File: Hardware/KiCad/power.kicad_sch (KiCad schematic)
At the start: 54 parts, among them U6 TP6841S6, U7 TPS73233

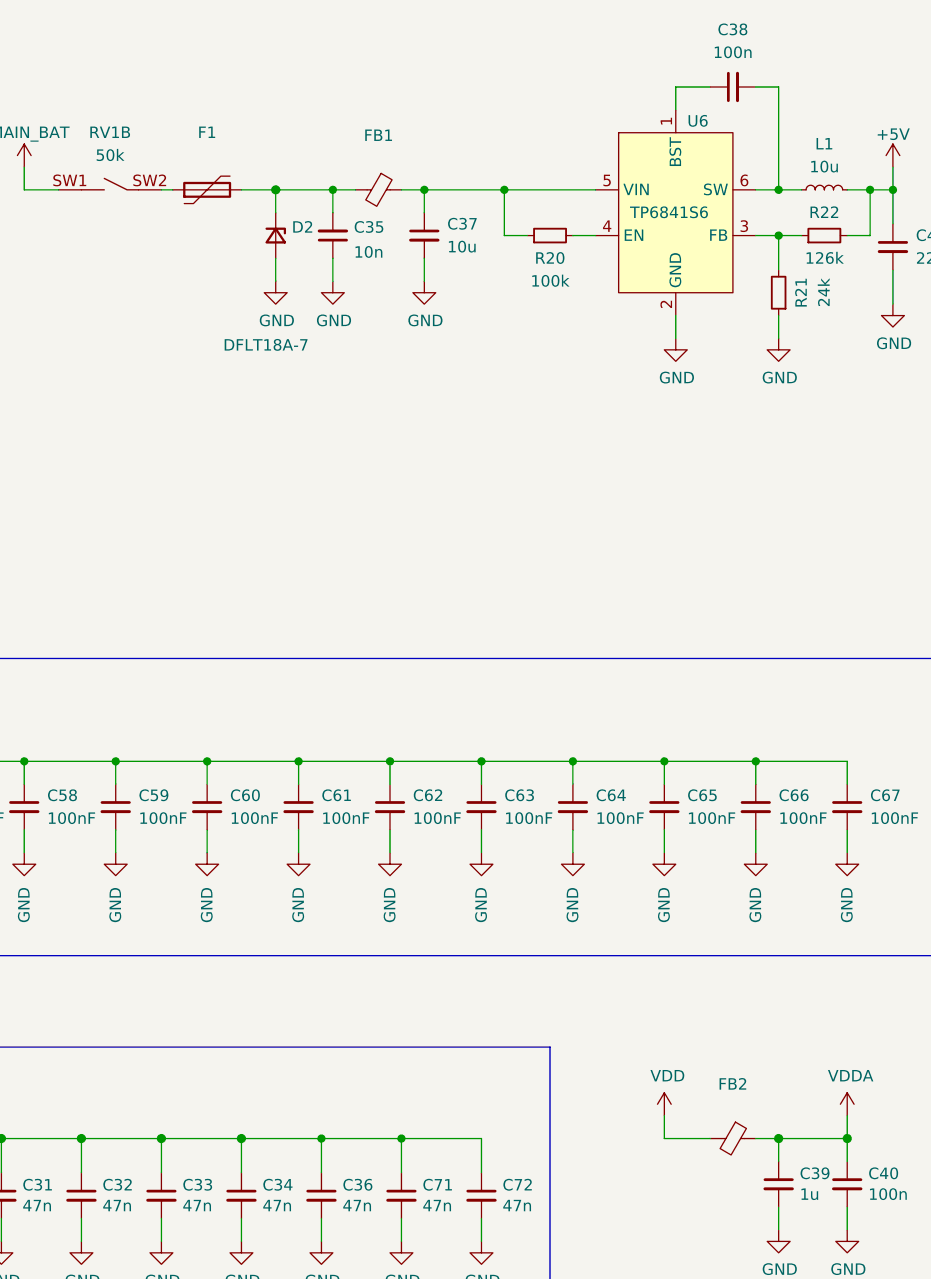
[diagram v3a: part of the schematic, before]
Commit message: move cc1200 spi to spi-5 & update other labels throughout
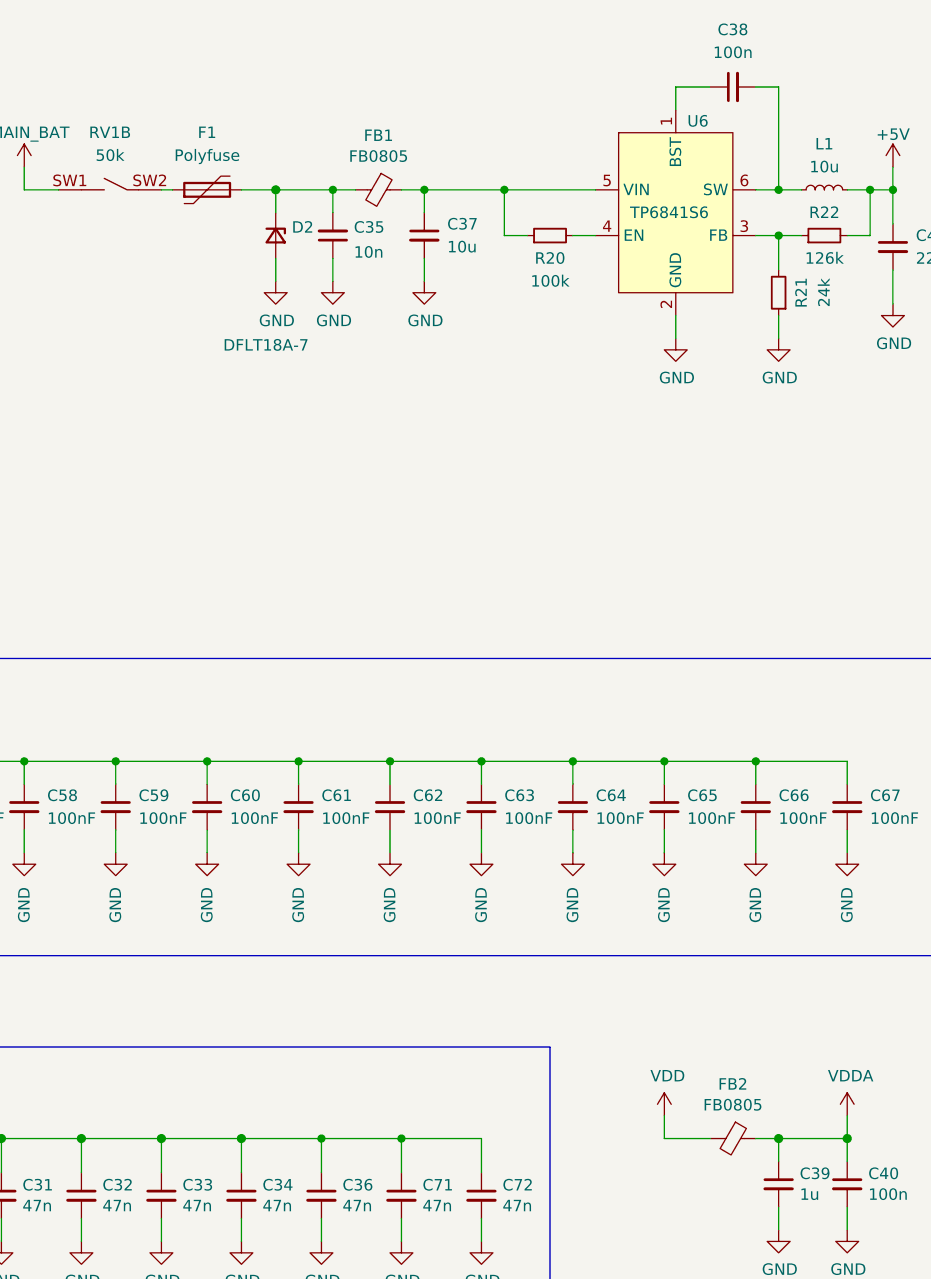
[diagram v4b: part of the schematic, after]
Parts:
- F1: value (none) -> Polyfuse; footprint (none) -> Fuse:Fuse_0805_2012Metric
- FB1, FB2: value (none) -> FB0805; footprint (none) -> Fuse:Fuse_0805_2012Metric
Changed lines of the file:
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@@
     (in_bom yes) (on_board yes)
     (property "Reference" "FB1" (id 0) (at 92.71 29.5402 90))
-    (property "Value" "" (id 1) (at 92.71 31.8516 90))
-    (property "Footprint" "" (id 2) (at 92.71 33.782 90)
+    (property "Value" "FB0805" (id 1) (at 92.71 31.8516 90))
+    (property "Footprint" "Fuse:Fuse_0805_2012Metric" (id 2) (at 92.71 33.782 90)
       (effects (font (size 1.27 1.27)) hide)
     )
@@
     (in_bom yes) (on_board yes) (fields_autoplaced)
     (property "Reference" "F1" (id 0) (at 73.66 29.21 90))
-    (property "Value" "" (id 1) (at 73.66 31.75 90))
-    (property "Footprint" "" (id 2) (at 78.74 34.29 0)
+    (property "Value" "Polyfuse" (id 1) (at 73.66 31.75 90))
+    (property "Footprint" "Fuse:Fuse_0805_2012Metric" (id 2) (at 78.74 34.29 0)
       (effects (font (size 1.27 1.27)) (justify left) hide)
     )
@@
     (in_bom yes) (on_board yes)
     (property "Reference" "FB2" (id 0) (at 132.08 134.9502 90))
-    (property "Value" "" (id 1) (at 132.08 137.2616 90))
-    (property "Footprint" "" (id 2) (at 132.08 139.192 90)
-      (effects (font (size 1.27 1.27)) hide)
-    )
+    (property "Value" "FB0805" (id 1) (at 132.08 137.2616 90))
+    (property "Footprint" "Fuse:Fuse_0805_2012Metric" (id 2) (at 132.08 139.192 90)
+      (effects (font (size 1.27 1.27)) hide)
+    )

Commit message: rough layout of cc1200
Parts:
- removed C29, C30, C31, C32, C33, C34, C36, C71, C72: 47n, Capacitor_SMD:C_0402_1005Metric, symbol pkl_device:pkl_C_Small
- C9: renamed from C61; value 100nF -> (none); footprint Capacitor_SMD:C_0402_1005Metric -> (none)
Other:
- note removed: "CC1200 decoupling"

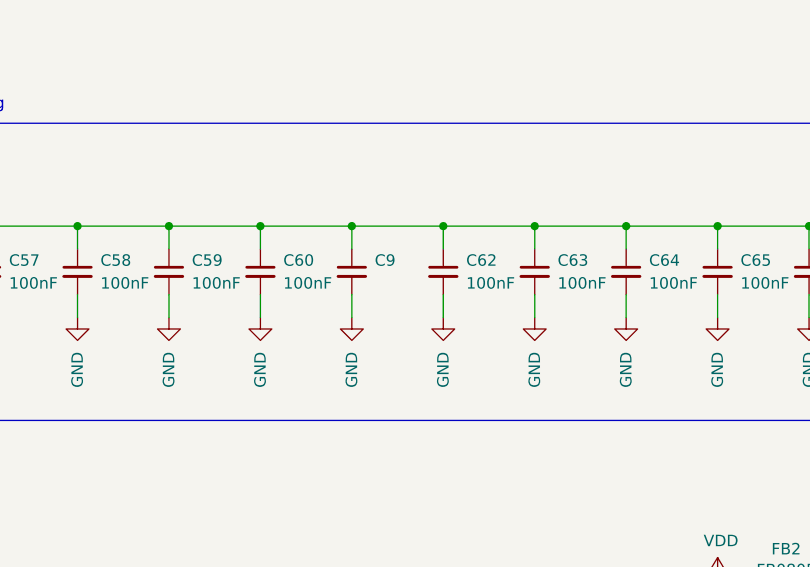
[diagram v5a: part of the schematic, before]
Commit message: fix issue 21 & 20 & move MCU to align w/ grid
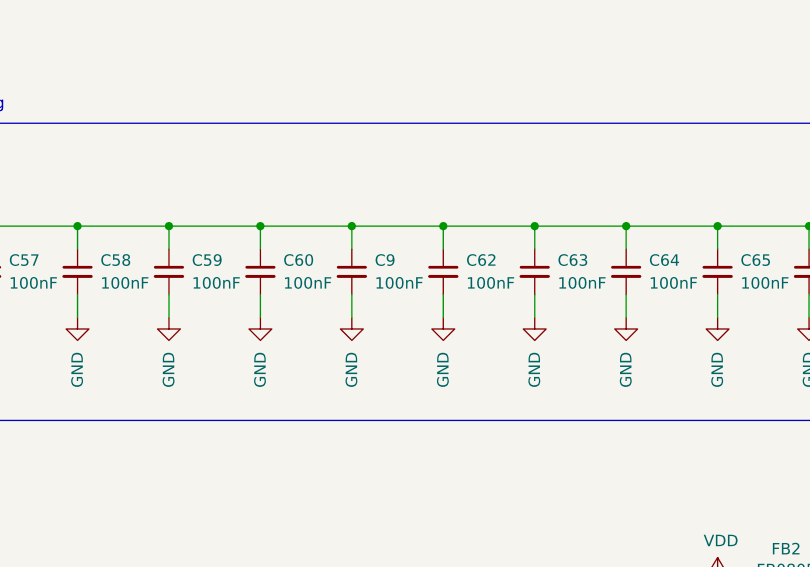
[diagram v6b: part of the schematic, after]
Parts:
- C9: value (none) -> 100nF; footprint (none) -> Capacitor_SMD:C_0402_1005Metric
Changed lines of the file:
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@@
       (effects (font (size 1.27 1.27)) (justify left))
     )
-    (property "Value" "" (id 1) (at 86.36 105.4162 0)
+    (property "Value" "100nF" (id 1) (at 86.36 105.4162 0)
       (effects (font (size 1.27 1.27)) (justify left))
     )
-    (property "Footprint" "" (id 2) (at 83.82 104.14 0)
+    (property "Footprint" "Capacitor_SMD:C_0402_1005Metric" (id 2) (at 83.82 104.14 0)
       (effects (font (size 1.27 1.27)) hide)
     )

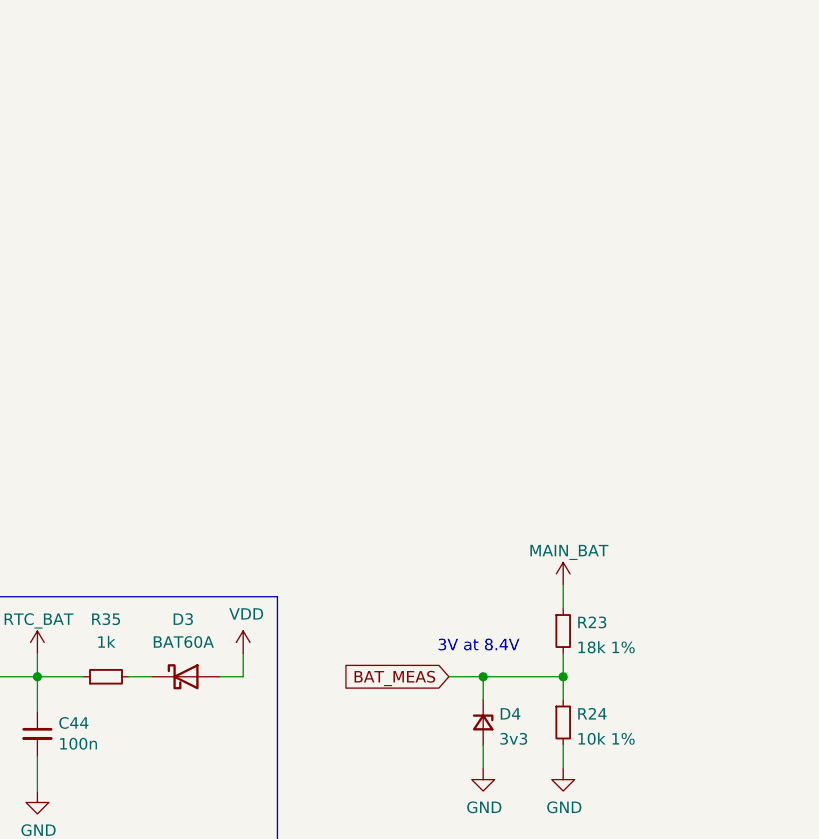
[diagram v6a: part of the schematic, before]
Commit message: Minor corrections
- fixed microphone connection and part values
- added a few TPs
- changed C27 footprint
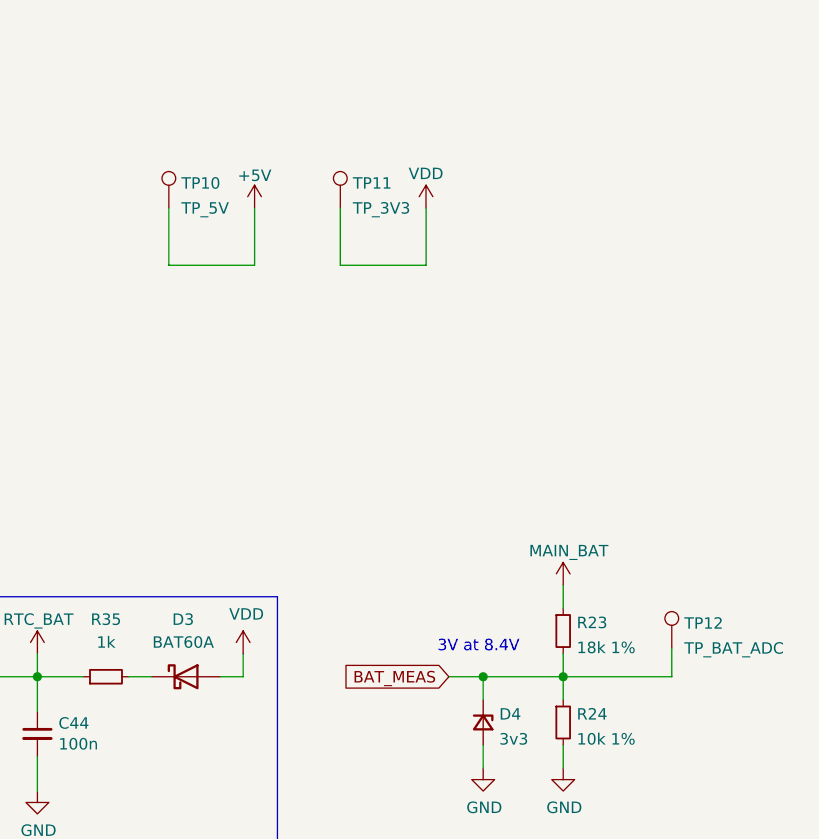
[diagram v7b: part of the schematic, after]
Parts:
- added TP10: TP_5V, TestPoint:TestPoint_Pad_D1.0mm, symbol Connector:TestPoint
- added TP11: TP_3V3, TestPoint:TestPoint_Pad_D1.0mm, symbol Connector:TestPoint
- added TP12: TP_BAT_ADC, TestPoint:TestPoint_Pad_D1.0mm, symbol Connector:TestPoint
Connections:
- net +5V: now also TP10.1
- net BAT_MEAS: now also TP12.1
- net VDD: now also TP11.1
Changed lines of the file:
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@@
     (stroke (width 0) (type solid) (color 0 0 0 0))
+  )
+  (wire (pts (xy 200.025 95.25) (xy 209.55 95.25))
+    (stroke (width 0) (type default) (color 0 0 0 0))
   )
   (wire (pts (xy 114.3 101.6) (xy 114.3 99.06))
@@
     (stroke (width 0) (type default) (color 0 0 0 0))
   )
+  (wire (pts (xy 200.025 88.9) (xy 200.025 95.25))
+    (stroke (width 0) (type default) (color 0 0 0 0))
+  )
+  (wire (pts (xy 255.905 137.795) (xy 255.905 140.97))
+    (stroke (width 0) (type default) (color 0 0 0 0))
+  )
   (wire (pts (xy 114.3 106.68) (xy 114.3 109.22))
     (stroke (width 0) (type default) (color 0 0 0 0))
@@
     (stroke (width 0) (type default) (color 0 0 0 0))
   )
+  (wire (pts (xy 228.6 95.25) (xy 228.6 88.9))
+    (stroke (width 0) (type default) (color 0 0 0 0))
+  )
   (wire (pts (xy 144.78 140.97) (xy 144.78 138.43))
     (stroke (width 0) (type solid) (color 0 0 0 0))
@@
     (stroke (width 0) (type default) (color 0 0 0 0))
   )
+  (wire (pts (xy 209.55 95.25) (xy 209.55 88.9))
+    (stroke (width 0) (type default) (color 0 0 0 0))
+  )
   (wire (pts (xy 104.14 99.06) (xy 114.3 99.06))
     (stroke (width 0) (type default) (color 0 0 0 0))
@@
     (stroke (width 0) (type solid) (color 0 0 0 0))
   )
+  (wire (pts (xy 219.075 88.9) (xy 219.075 95.25))
+    (stroke (width 0) (type default) (color 0 0 0 0))
+  )
   (wire (pts (xy 125.73 24.13) (xy 125.73 26.67))
     (stroke (width 0) (type default) (color 0 0 0 0))
   )
+  (wire (pts (xy 219.075 95.25) (xy 228.6 95.25))
+    (stroke (width 0) (type default) (color 0 0 0 0))
+  )
   (polyline (pts (xy 170.18 132.08) (xy 212.09 132.08))
     (stroke (width 0) (type default) (color 0 0 0 0))
@@
   (wire (pts (xy 87.63 35.56) (xy 87.63 38.1))
     (stroke (width 0) (type solid) (color 0 0 0 0))
+  )
+  (wire (pts (xy 255.905 140.97) (xy 243.84 140.97))
+    (stroke (width 0) (type default) (color 0 0 0 0))
   )
   (wire (pts (xy 167.64 35.56) (xy 167.64 33.02))
@@
     (pin "1")
   )
+  (symbol (lib_id "Connector:TestPoint") (at 255.905 137.795 0) (unit 1)
+    (in_bom yes) (on_board yes) (fields_autoplaced)
+    (property "Reference" "TP12" (id 0) (at 257.3021 135.045 0)
+      (effects (font (size 1.27 1.27)) (justify left))
+    )
+    (property "Value" "TP_BAT_ADC" (id 1) (at 257.3021 137.8201 0)
+      (effects (font (size 1.27 1.27)) (justify left))
+    )
+    (property "Footprint" "TestPoint:TestPoint_Pad_D1.0mm" (id 2) (at 260.985 137.795 0)
+      (effects (font (size 1.27 1.27)) hide)
+    )
+    (property "Datasheet" "~" (id 3) (at 260.985 137.795 0)
+      (effects (font (size 1.27 1.27)) hide)
+    )
+    (pin "1")
+  )
   (symbol (lib_id "power:GND") (at 87.63 45.72 0) (unit 1)
     (in_bom yes) (on_board yes)
@@
     (pin "1")
   )
+  (symbol (lib_id "power:+5V") (at 209.55 88.9 0) (unit 1)
+    (in_bom yes) (on_board yes) (fields_autoplaced)
+    (property "Reference" "#PWR08" (id 0) (at 209.55 92.71 0)
+      (effects (font (size 1.27 1.27)) hide)
+    )
+    (property "Value" "+5V" (id 1) (at 209.55 85.2954 0))
+    (property "Footprint" "" (id 2) (at 209.55 88.9 0)
+      (effects (font (size 1.27 1.27)) hide)
+    )
+    (property "Datasheet" "" (id 3) (at 209.55 88.9 0)
+      (effects (font (size 1.27 1.27)) hide)
+    )
+    (pin "1")
+  )
   (symbol (lib_id "Device:Ferrite_Bead_Small") (at 132.08 140.97 270) (unit 1)
     (in_bom yes) (on_board yes)
@@
     (pin "1")
   )
+  (symbol (lib_id "Connector:TestPoint") (at 219.075 88.9 0) (unit 1)
+    (in_bom yes) (on_board yes) (fields_autoplaced)
+    (property "Reference" "TP11" (id 0) (at 220.4721 86.15 0)
+      (effects (font (size 1.27 1.27)) (justify left))
+    )
+    (property "Value" "TP_3V3" (id 1) (at 220.4721 88.9251 0)
+      (effects (font (size 1.27 1.27)) (justify left))
+    )
+    (property "Footprint" "TestPoint:TestPoint_Pad_D1.0mm" (id 2) (at 224.155 88.9 0)
+      (effects (font (size 1.27 1.27)) hide)
+    )
+    (property "Datasheet" "~" (id 3) (at 224.155 88.9 0)
+      (effects (font (size 1.27 1.27)) hide)
+    )
+    (pin "1")
+  )
+  (symbol (lib_id "power:VDD") (at 228.6 88.9 0) (unit 1)
+    (in_bom yes) (on_board yes)
+    (property "Reference" "#PWR09" (id 0) (at 228.6 92.71 0)
+      (effects (font (size 1.27 1.27)) hide)
+    )
+    (property "Value" "VDD" (id 1) (at 228.6 85.09 0))
+    (property "Footprint" "" (id 2) (at 228.6 88.9 0)
+      (effects (font (size 1.27 1.27)) hide)
+    )
+    (property "Datasheet" "" (id 3) (at 228.6 88.9 0)
+      (effects (font (size 1.27 1.27)) hide)
+    )
+    (pin "1")
+  )
   (symbol (lib_id "power:GND") (at 114.3 109.22 0) (unit 1)
     (in_bom yes) (on_board yes) (fields_autoplaced)
@@
       (effects (font (size 1.27 1.27)) hide)
     )
+    (pin "1")
+  )
+  (symbol (lib_id "Connector:TestPoint") (at 200.025 88.9 0) (unit 1)
+    (in_bom yes) (on_board yes) (fields_autoplaced)
+    (property "Reference" "TP10" (id 0) (at 201.4221 86.15 0)
+      (effects (font (size 1.27 1.27)) (justify left))
+    )
+    (property "Value" "TP_5V" (id 1) (at 201.4221 88.9251 0)
+      (effects (font (size 1.27 1.27)) (justify left))
+    )
+    (property "Footprint" "TestPoint:TestPoint_Pad_D1.0mm" (id 2) (at 205.105 88.9 0)
+      (effects (font (size 1.27 1.27)) hide)
+    )
+    (property "Datasheet" "~" (id 3) (at 205.105 88.9 0)
+      (effects (font (size 1.27 1.27)) hide)
+    )
